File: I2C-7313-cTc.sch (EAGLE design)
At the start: 75 parts, among them CON1 CONNECTOR-I2CLEFT, CON2 CONNECTOR-I2CLEFT, IC1 MAX7313AEG, IC2 MAX7313AEG, SW1 CTC-6PDT, SW2 CTC-4P3T, SW3 CTC-4P3T, SW4 CTC-6PDT

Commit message: normalized values
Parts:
- AD0, AD1, AD2, AD3, AD4, AD5, I2C-CABLE, I2C-CABLE1: value (none) -> 2x4-0.100
- BOARD1: value (none) -> BOARD
- CODEBUTTON, CODEBUTTON1, MCLED, MCLED1, MODBOARDLEDS, MODBOARDLEDS1: value (none) -> 0.100
- CON1, CON2: value CONNECTOR-I2CLEFT -> I2C
- MCSWITCH, MCSWITCH1: value (none) -> 0.200
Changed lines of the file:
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@@
 <setting verticaltext="up"/>
 </settings>
-<grid distance="0.1" unitdist="inch" unit="inch" style="lines" multiple="1" display="no" altdistance="0.01" altunitdist="inch" altunit="inch"/>
+<grid distance="100" unitdist="mil" unit="mil" style="dots" multiple="1" display="yes" altdistance="50" altunitdist="mil" altunit="mil"/>
 <layers>
 <layer number="1" name="Top" color="4" fill="1" visible="no" active="no"/>
@@
 <part name="GND3" library="supply1" deviceset="GND" device=""/>
 <part name="R6" library="SPCoast" deviceset="R*" device="0805-RES" value="82R"/>
-<part name="MCLED" library="SPCoast" deviceset="JUMPER-2" device="PTH_LOCK"/>
-<part name="MODBOARDLEDS" library="SPCoast" deviceset="CONNECTOR-M06" device="LOCK_LONGPADS"/>
+<part name="MCLED" library="SPCoast" deviceset="JUMPER-2" device="PTH_LOCK" value="0.100"/>
+<part name="MODBOARDLEDS" library="SPCoast" deviceset="CONNECTOR-M06" device="LOCK_LONGPADS" value="0.100"/>
 <part name="R7" library="SPCoast" deviceset="R*" device="0805-RES" value="82R"/>
 <part name="R8" library="SPCoast" deviceset="R*" device="0805-RES" value="82R"/>
 <part name="R9" library="SPCoast" deviceset="R*" device="0805-RES" value="82R"/>
-<part name="CON1" library="SPCoast" deviceset="CONNECTOR-I2C" device="LEFT"/>
-<part name="MCSWITCH" library="SPCoast" deviceset="CONNECTOR-M02" device="5MM-LOCK"/>
+<part name="CON1" library="SPCoast" deviceset="CONNECTOR-I2C" device="LEFT" value="I2C"/>
+<part name="MCSWITCH" library="SPCoast" deviceset="CONNECTOR-M02" device="5MM-LOCK" value="0.200"/>
 <part name="GND12" library="supply1" deviceset="GND" device=""/>
-<part name="CODEBUTTON" library="SPCoast" deviceset="CONNECTOR-M02" device="1X02-LOCK"/>
+<part name="CODEBUTTON" library="SPCoast" deviceset="CONNECTOR-M02" device="1X02-LOCK" value="0.100"/>
 <part name="GND13" library="supply1" deviceset="GND" device=""/>
 <part name="IC1" library="maxim" deviceset="MAX7313AEG" device=""/>
-<part name="I2C-CABLE" library="con-lstb" deviceset="MA04-2" device=""/>
-<part name="AD0" library="con-lstb" deviceset="MA04-2" device=""/>
-<part name="AD1" library="con-lstb" deviceset="MA04-2" device=""/>
-<part name="AD2" library="con-lstb" deviceset="MA04-2" device=""/>
+<part name="I2C-CABLE" library="con-lstb" deviceset="MA04-2" device="" value="2x4-0.100"/>
+<part name="AD0" library="con-lstb" deviceset="MA04-2" device="" value="2x4-0.100"/>
+<part name="AD1" library="con-lstb" deviceset="MA04-2" device="" value="2x4-0.100"/>
+<part name="AD2" library="con-lstb" deviceset="MA04-2" device="" value="2x4-0.100"/>
 <part name="VR1" library="SPCoast" deviceset="VREG_LM1117" device="SOT223" value="3v3"/>
 <part name="+3V1" library="supply1" deviceset="+3V3" device=""/>
@@
 <part name="GND10" library="supply1" deviceset="GND" device=""/>
 <part name="R22" library="SPCoast" deviceset="R*" device="0805-RES" value="82R"/>
-<part name="MCLED1" library="SPCoast" deviceset="JUMPER-2" device="PTH_LOCK"/>
-<part name="MODBOARDLEDS1" library="SPCoast" deviceset="CONNECTOR-M06" device="LOCK_LONGPADS"/>
+<part name="MCLED1" library="SPCoast" deviceset="JUMPER-2" device="PTH_LOCK" value="0.100"/>
+<part name="MODBOARDLEDS1" library="SPCoast" deviceset="CONNECTOR-M06" device="LOCK_LONGPADS" value="0.100"/>
 <part name="R23" library="SPCoast" deviceset="R*" device="0805-RES" value="82R"/>
 <part name="R24" library="SPCoast" deviceset="R*" device="0805-RES" value="82R"/>
 <part name="R25" library="SPCoast" deviceset="R*" device="0805-RES" value="82R"/>
-<part name="CON2" library="SPCoast" deviceset="CONNECTOR-I2C" device="LEFT"/>
-<part name="MCSWITCH1" library="SPCoast" deviceset="CONNECTOR-M02" device="5MM-LOCK"/>
+<part name="CON2" library="SPCoast" deviceset="CONNECTOR-I2C" device="LEFT" value="I2C"/>
+<part name="MCSWITCH1" library="SPCoast" deviceset="CONNECTOR-M02" device="5MM-LOCK" value="0.200"/>
 <part name="GND11" library="supply1" deviceset="GND" device=""/>
-<part name="CODEBUTTON1" library="SPCoast" deviceset="CONNECTOR-M02" device="1X02-LOCK"/>
+<part name="CODEBUTTON1" library="SPCoast" deviceset="CONNECTOR-M02" device="1X02-LOCK" value="0.100"/>
 <part name="GND14" library="supply1" deviceset="GND" device=""/>
 <part name="IC2" library="maxim" deviceset="MAX7313AEG" device=""/>
-<part name="I2C-CABLE1" library="con-lstb" deviceset="MA04-2" device=""/>
-<part name="AD3" library="con-lstb" deviceset="MA04-2" device=""/>
-<part name="AD4" library="con-lstb" deviceset="MA04-2" device=""/>
-<part name="AD5" library="con-lstb" deviceset="MA04-2" device=""/>
+<part name="I2C-CABLE1" library="con-lstb" deviceset="MA04-2" device="" value="2x4-0.100"/>
+<part name="AD3" library="con-lstb" deviceset="MA04-2" device="" value="2x4-0.100"/>
+<part name="AD4" library="con-lstb" deviceset="MA04-2" device="" value="2x4-0.100"/>
+<part name="AD5" library="con-lstb" deviceset="MA04-2" device="" value="2x4-0.100"/>
 <part name="VR2" library="SPCoast" deviceset="VREG_LM1117" device="SOT223" value="3v3"/>
 <part name="+3V12" library="supply1" deviceset="+3V3" device=""/>
@@
 <part name="GND18" library="supply1" deviceset="GND" device=""/>
 <part name="+3V22" library="supply1" deviceset="+3V3" device=""/>
-<part name="BOARD1" library="SPCoast" deviceset="BOARD" device="100X150X2-NOHOLES"/>
+<part name="BOARD1" library="SPCoast" deviceset="BOARD" device="100X150X2-NOHOLES" value="BOARD"/>
 </parts>
 <sheets>

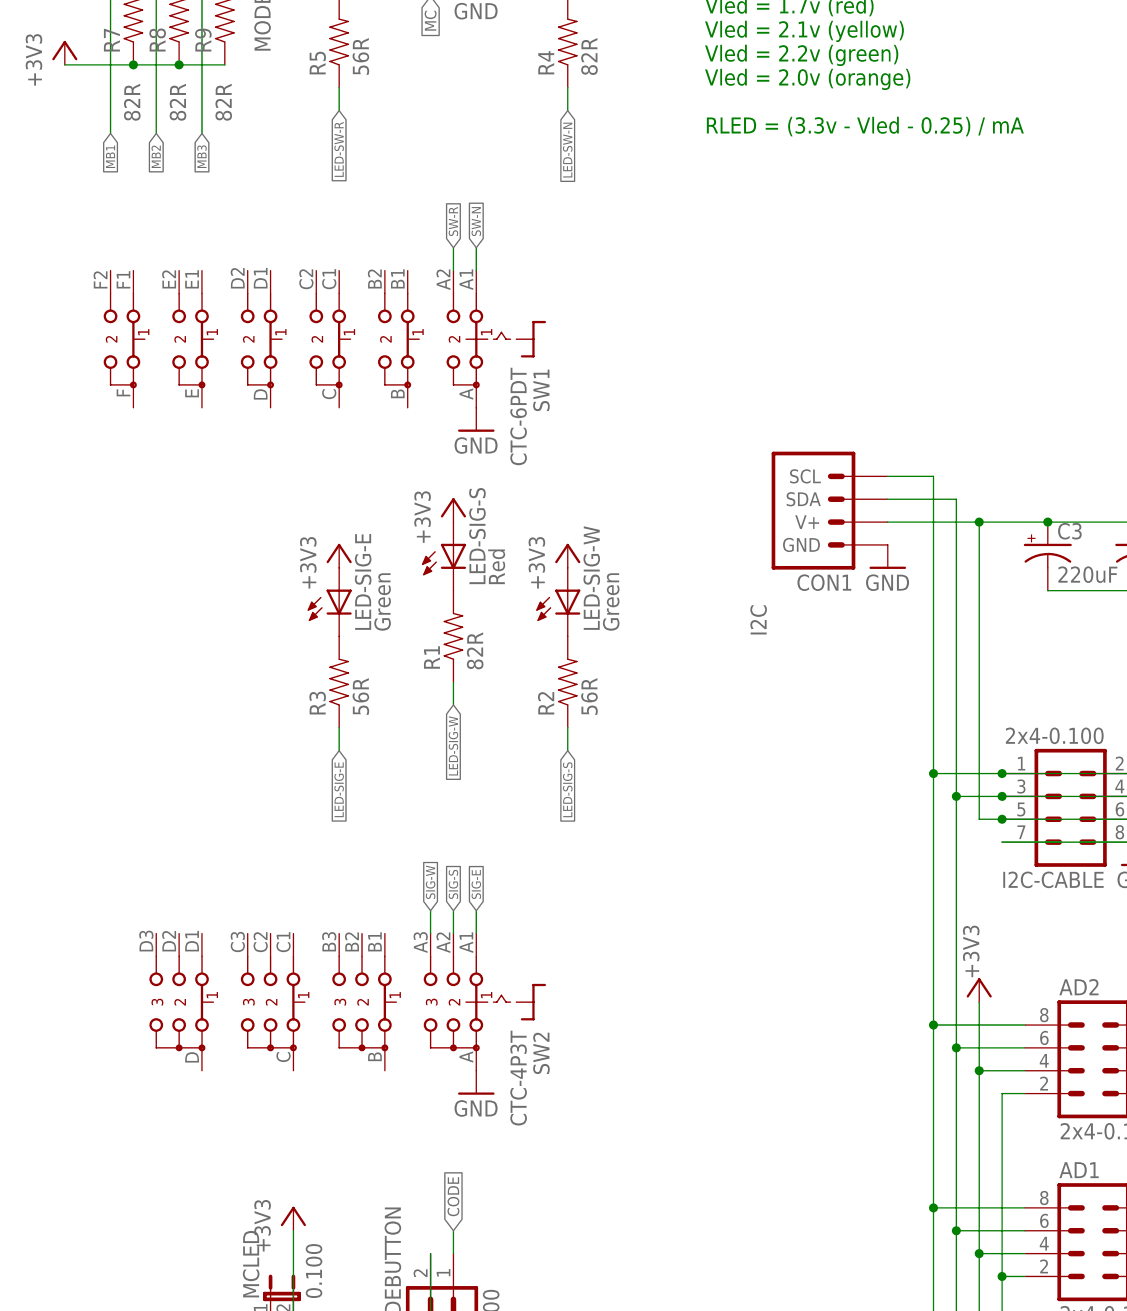
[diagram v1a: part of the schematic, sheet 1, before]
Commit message: replaced 4PDT rotary with 2P2T SR2616F-0202-18F58-D8-N
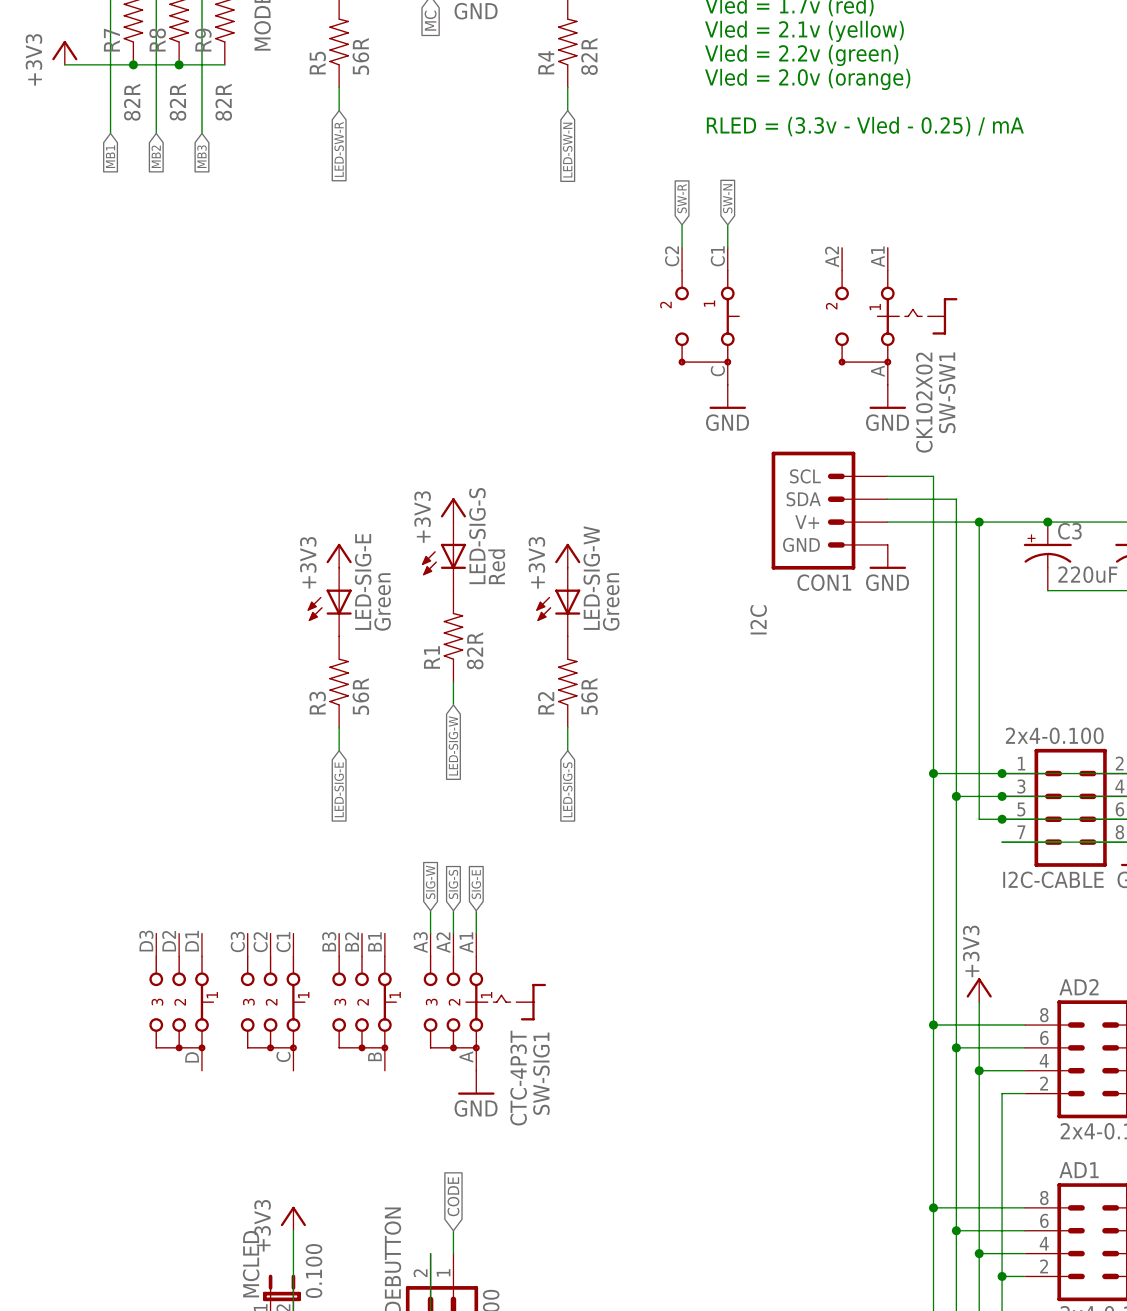
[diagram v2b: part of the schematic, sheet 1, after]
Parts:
- removed SW1, SW4: CTC-6PDT, SPCoast:CTC-6PDT
- added SW-SW1, SW-SW2: CK102X02, SPCoast:CK102X02
- C1, C2, C4, C5: device SPCoast:CAP0805 -> SPCoast:CAP0603
- C3, C6: device SPCoast:CAP-POLPTH-5MM -> SPCoast:CAP-POL0810
- R1, R10, R11, R12, R13, R14, R15, R16, R17, R18, R19, R2, R20, R21, R22, R23, R24, R25, R26, R27, R28, R29, R3, R30, R31, R32, R4, R5, R6, R7, R8, R9: device SPCoast:R0805-RES -> SPCoast:R0603-RES
- renumbered SW2 to SW-SIG1, SW3 to SW-SIG2
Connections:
- net CODE: now also CODEBUTTON.A, CODEBUTTON1.A; no longer CODEBUTTON.1, CODEBUTTON1.1
- net GND: now also CODEBUTTON.B, CODEBUTTON1.B, MCSWITCH.B, MCSWITCH1.B, SW-SW1.A, SW-SW1.C, SW-SW2.A, SW-SW2.C; no longer CODEBUTTON.2, CODEBUTTON1.2, MCSWITCH.2, MCSWITCH1.2, SW1.A, SW4.A
- net MC: now also MCSWITCH.A, MCSWITCH1.A; no longer MCSWITCH.1, MCSWITCH1.1
- net SW-N: now also SW-SW1.C1, SW-SW2.C1; no longer SW1.A1, SW4.A1
- net SW-R: now also SW-SW1.C2, SW-SW2.C2; no longer SW1.A2, SW4.A2

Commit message: Version 2.2
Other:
- note added: "2.2"
- moved on the sheet: SW-SW1
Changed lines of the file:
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@@
 <text x="149.86" y="20.32" size="2.1844" layer="91">cTc Panel Wiring Simplifier
 I2C switch and LED interface</text>
-<text x="239.268" y="13.462" size="2.1844" layer="91">2.1</text>
+<text x="239.268" y="13.462" size="2.1844" layer="91">2.2</text>
 <text x="240.284" y="6.858" size="2.1844" layer="91">B</text>
 <text x="144.78" y="139.7" size="1.778" layer="91" font="fixed">Red/Orange/Yellow       82
@@
 </instance>
 <instance part="BOARD1" gate="B" x="238.76" y="33.02"/>
-<instance part="SW-SW1" gate="SW1" x="86.36" y="134.62" rot="R180"/>
-<instance part="GND19" gate="1" x="99.06" y="124.46"/>
-<instance part="GND9" gate="1" x="81.28" y="124.46"/>
+<instance part="SW-SW1" gate="SW1" x="55.88" y="132.08" rot="R180"/>
+<instance part="GND19" gate="1" x="68.58" y="121.92"/>
+<instance part="GND9" gate="1" x="50.8" y="121.92"/>
 </instances>
 <busses>
@@
 </segment>
 <segment>
-<wire x1="81.28" y1="142.24" x2="81.28" y2="144.78" width="0.1524" layer="91"/>
-<label x="81.28" y="144.78" size="1.016" layer="95" rot="R90" xref="yes"/>
+<wire x1="50.8" y1="139.7" x2="50.8" y2="142.24" width="0.1524" layer="91"/>
+<label x="50.8" y="142.24" size="1.016" layer="95" rot="R90" xref="yes"/>
 <pinref part="SW-SW1" gate="SW1" pin="C1"/>
 </segment>
@@
 </segment>
 <segment>
-<wire x1="76.2" y1="142.24" x2="76.2" y2="144.78" width="0.1524" layer="91"/>
-<label x="76.2" y="144.78" size="1.016" layer="95" rot="R90" xref="yes"/>
+<wire x1="45.72" y1="139.7" x2="45.72" y2="142.24" width="0.1524" layer="91"/>
+<label x="45.72" y="142.24" size="1.016" layer="95" rot="R90" xref="yes"/>
 <pinref part="SW-SW1" gate="SW1" pin="C2"/>
 </segment>
